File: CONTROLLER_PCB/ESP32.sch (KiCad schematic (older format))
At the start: 3 parts

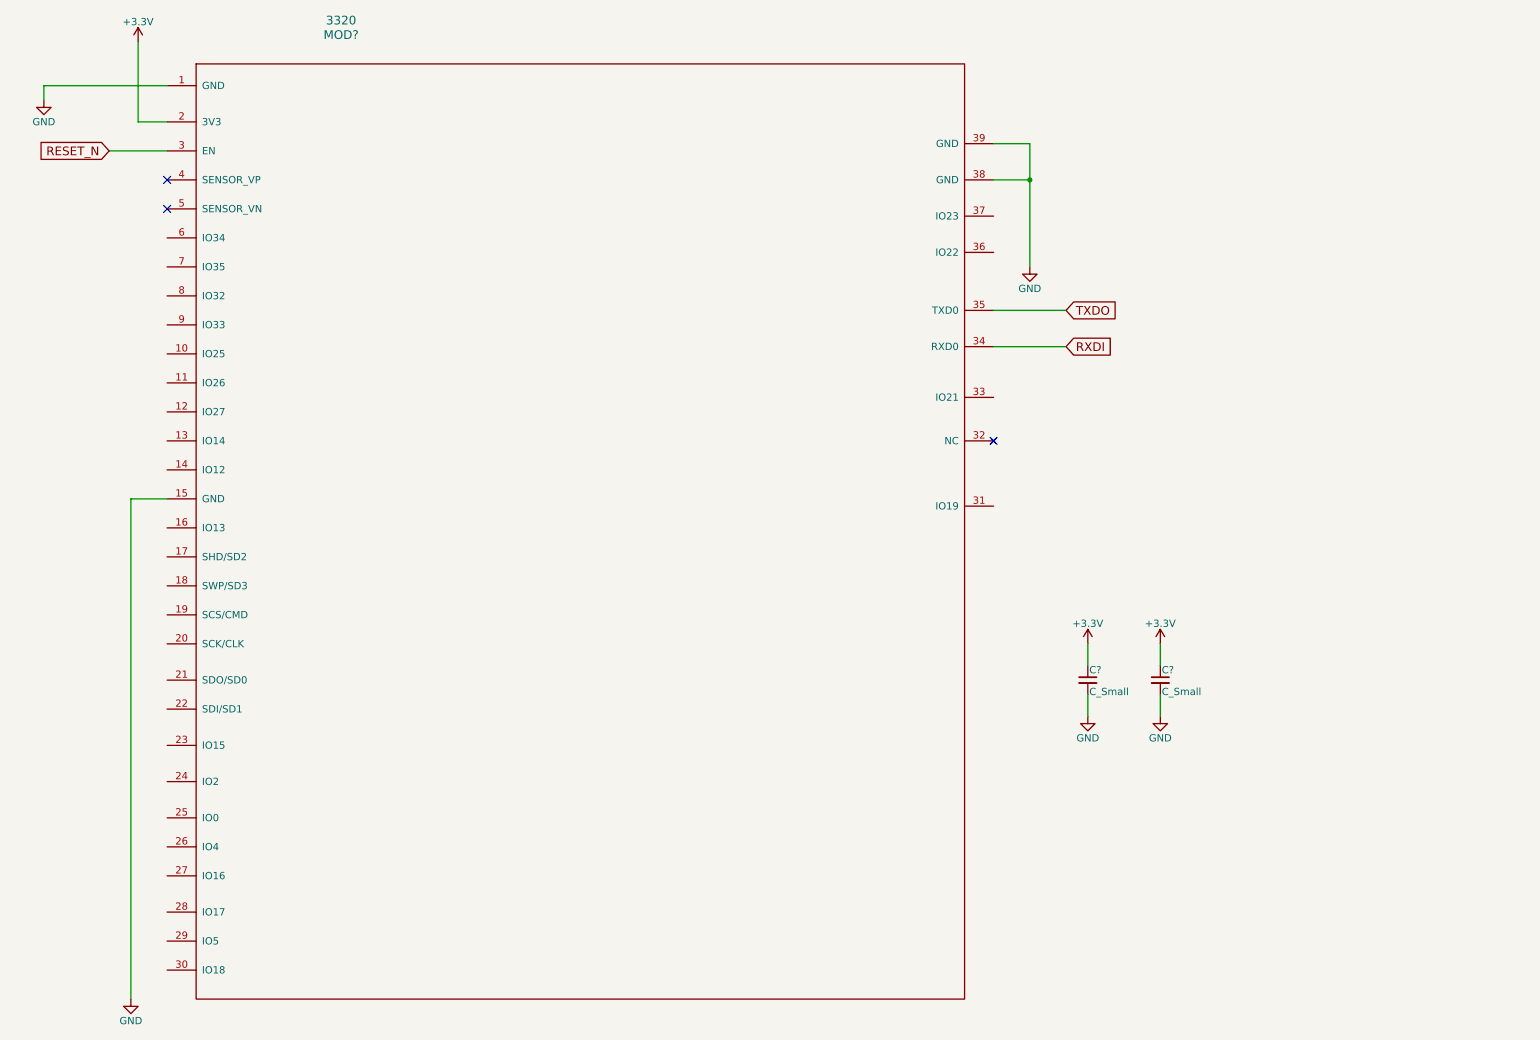
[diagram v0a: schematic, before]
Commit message: Created ESP32 pinout spreadsheet, finished MCU pinout, and added MCU_SUPPORT schematic sheet.
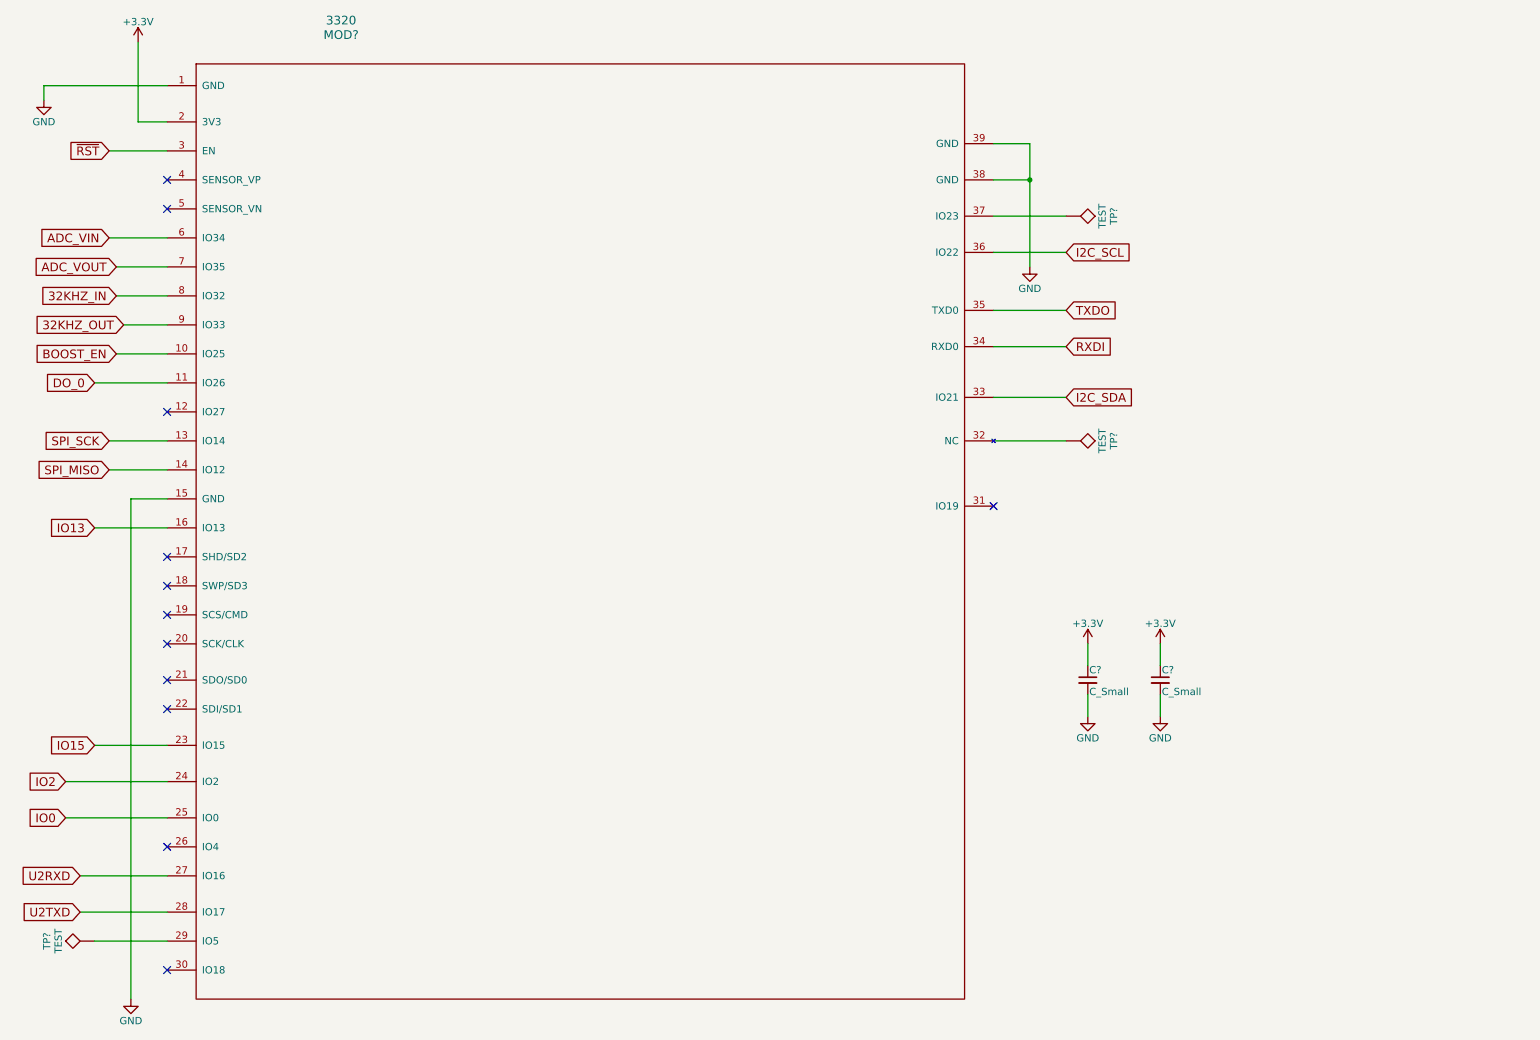
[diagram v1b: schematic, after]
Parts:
- added TP? (x3): TEST, symbol TEST
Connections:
- net BOOST_EN: now reaches MOD?.10 (IO25)
- net DO_0: now reaches MOD?.11 (IO26)
- net SPI_SCK: now reaches MOD?.13 (IO14)
- net SPI_MISO: now reaches MOD?.14 (IO12)
- net IO13: now reaches MOD?.16 (IO13)
- net IO15: now reaches MOD?.23 (IO15)
- net IO2: now reaches MOD?.24 (IO2)
- net IO0: now reaches MOD?.25 (IO0)
- net U2RXD: now reaches MOD?.27 (IO16)
- net U2TXD: now reaches MOD?.28 (IO17)
- net at MOD?.29 (IO5): now also TP?.1
- net at MOD?.32 (NC): now also TP?.1
- net I2C_SDA: now reaches MOD?.33 (IO21)
- net I2C_SCL: now reaches MOD?.36 (IO22)
- net at MOD?.37 (IO23): now also TP?.1
- net ADC_VIN: now reaches MOD?.6 (IO34)
- net ADC_VOUT: now reaches MOD?.7 (IO35)
- net 32KHZ_IN: now reaches MOD?.8 (IO32)
- net 32KHZ_OUT: now reaches MOD?.9 (IO33)
- net RESET_N renamed ~RST
- no-connect marks 3 -> 12
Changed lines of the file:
@@
 $Descr A4 11693 8268
 encoding utf-8
-Sheet 3 3
+Sheet 3 4
 Title ""
 Date ""
@@
 Comment4 ""
 $EndDescr
+$Comp
+L GND #PWR?
+U 1 1 5C5A52E4
+P 600 1150
+F 0 "#PWR?" H 600 900 50  0001 C CNN
+F 1 "GND" H 600 1000 50  0000 C CNN
+F 2 "" H 600 1150 50  0001 C CNN
+F 3 "" H 600 1150 50  0001 C CNN
+	1    600  1150
+	1    0    0    -1
+$EndComp
+$Comp
+L +3.3V #PWR?
+U 1 1 5C5AB14D
+P 1250 750
+F 0 "#PWR?" H 1250 600 50  0001 C CNN
+F 1 "+3.3V" H 1250 890 50  0000 C CNN
+F 2 "" H 1250 750 50  0001 C CNN
+F 3 "" H 1250 750 50  0001 C CNN
+	1    1250 750
+	1    0    0    -1
+$EndComp
+Text GLabel 1050 1500 0    60   Input ~ 0
+~RST
+NoConn ~ 1450 1700
+NoConn ~ 1450 1900
+Wire Wire Line
+	1050 1500 1450 1500
+Wire Wire Line
+	1450 1300 1250 1300
+Wire Wire Line
+	1250 1300 1250 750
+Wire Wire Line
+	1450 1050 600  1050
+Wire Wire Line
+	600  1050 600  1150
+$Comp
+L GND #PWR?
+U 1 1 5C5AB35F
+P 7400 2300
+F 0 "#PWR?" H 7400 2050 50  0001 C CNN
+F 1 "GND" H 7400 2150 50  0000 C CNN
+F 2 "" H 7400 2300 50  0001 C CNN
+F 3 "" H 7400 2300 50  0001 C CNN
+	1    7400 2300
+	1    0    0    -1
+$EndComp
+Wire Wire Line
+	7400 2300 7400 1450
+Wire Wire Line
+	7400 1450 7150 1450
+Wire Wire Line
+	7150 1700 7400 1700
+Connection ~ 7400 1700
+$Comp
+L GND #PWR?
+U 1 1 5C5AB3CE
+P 1200 7350
+F 0 "#PWR?" H 1200 7100 50  0001 C CNN
+F 1 "GND" H 1200 7200 50  0000 C CNN
+F 2 "" H 1200 7350 50  0001 C CNN
+F 3 "" H 1200 7350 50  0001 C CNN
+	1    1200 7350
+	1    0    0    -1
+$EndComp
+Wire Wire Line
+	1200 7350 1200 3900
+Wire Wire Line
+	1200 3900 1450 3900
+Text GLabel 7650 2600 2    60   Input ~ 0
+TXDO
+Text GLabel 7650 2850 2    60   Input ~ 0
+RXDI
+Wire Wire Line
+	7650 2850 7150 2850
+Wire Wire Line
+	7650 2600 7150 2600
+$Comp
+L C_Small C?
+U 1 1 5C5AC1FB
+P 7800 5150
+F 0 "C?" H 7810 5220 50  0000 L CNN
+F 1 "C_Small" H 7810 5070 50  0000 L CNN
+F 2 "" H 7800 5150 50  0001 C CNN
+F 3 "" H 7800 5150 50  0001 C CNN
+	1    7800 5150
+	1    0    0    -1
+$EndComp
+$Comp
+L C_Small C?
+U 1 1 5C5AC279
+P 8300 5150
+F 0 "C?" H 8310 5220 50  0000 L CNN
+F 1 "C_Small" H 8310 5070 50  0000 L CNN
+F 2 "" H 8300 5150 50  0001 C CNN
+F 3 "" H 8300 5150 50  0001 C CNN
+	1    8300 5150
+	1    0    0    -1
+$EndComp
+$Comp
+L GND #PWR?
+U 1 1 5C5AC2C0
+P 7800 5400
+F 0 "#PWR?" H 7800 5150 50  0001 C CNN
+F 1 "GND" H 7800 5250 50  0000 C CNN
+F 2 "" H 7800 5400 50  0001 C CNN
+F 3 "" H 7800 5400 50  0001 C CNN
+	1    7800 5400
+	1    0    0    -1
+$EndComp
+$Comp
+L GND #PWR?
+U 1 1 5C5AC2DA
+P 8300 5400
+F 0 "#PWR?" H 8300 5150 50  0001 C CNN
+F 1 "GND" H 8300 5250 50  0000 C CNN
+F 2 "" H 8300 5400 50  0001 C CNN
+F 3 "" H 8300 5400 50  0001 C CNN
+	1    8300 5400
+	1    0    0    -1
+$EndComp
+$Comp
+L +3.3V #PWR?
+U 1 1 5C5AC2F4
+P 7800 4900
+F 0 "#PWR?" H 7800 4750 50  0001 C CNN
+F 1 "+3.3V" H 7800 5040 50  0000 C CNN
+F 2 "" H 7800 4900 50  0001 C CNN
+F 3 "" H 7800 4900 50  0001 C CNN
+	1    7800 4900
+	1    0    0    -1
+$EndComp
+$Comp
+L +3.3V #PWR?
+U 1 1 5C5AC30E
+P 8300 4900
+F 0 "#PWR?" H 8300 4750 50  0001 C CNN
+F 1 "+3.3V" H 8300 5040 50  0000 C CNN
+F 2 "" H 8300 4900 50  0001 C CNN
+F 3 "" H 8300 4900 50  0001 C CNN
+	1    8300 4900
+	1    0    0    -1
+$EndComp
+Wire Wire Line
+	7800 5050 7800 4900
+Wire Wire Line
+	8300 5050 8300 4900
+Wire Wire Line
+	8300 5250 8300 5400
+Wire Wire Line
+	7800 5250 7800 5400
+Text GLabel 1050 2100 0    60   Input ~ 0
+ADC_VIN
+Text GLabel 1100 2300 0    60   Input ~ 0
+ADC_VOUT
+Wire Wire Line
+	1050 2100 1450 2100
+Wire Wire Line
+	1100 2300 1450 2300
+Text GLabel 1100 2500 0    60   Input ~ 0
+32KHZ_IN
+Text GLabel 1150 2700 0    60   Input ~ 0
+32KHZ_OUT
+Wire Wire Line
+	1100 2500 1450 2500
+Wire Wire Line
+	1150 2700 1450 2700
+Text GLabel 1100 2900 0    60   Input ~ 0
+BOOST_EN
+Wire Wire Line
+	1100 2900 1450 2900
+Text GLabel 950  3100 0    60   Input ~ 0
+DO_0
+Wire Wire Line
+	950  3100 1450 3100
+NoConn ~ 1450 3300
+Text GLabel 1050 3500 0    60   Input ~ 0
+SPI_SCK
+Text GLabel 1050 3700 0    60   Input ~ 0
+SPI_MISO
+Text GLabel 950  4100 0    60   Input ~ 0
+IO13
+Wire Wire Line
+	1050 3500 1450 3500
+Wire Wire Line
+	1050 3700 1450 3700
+Wire Wire Line
+	950  4100 1450 4100
+NoConn ~ 1450 4300
+NoConn ~ 1450 4500
+NoConn ~ 1450 4700
+NoConn ~ 1450 4900
+NoConn ~ 1450 5150
+NoConn ~ 1450 5350
+$Comp
+L TEST TP?
+U 1 1 5C5F05AF
+P 950 6950
+F 0 "TP?" H 950 7250 50  0000 C BNN
+F 1 "TEST" H 950 7200 50  0000 C CNN
+F 2 "" H 950 6950 50  0001 C CNN
+F 3 "" H 950 6950 50  0001 C CNN
+	1    950  6950
+	0    -1   -1   0
+$EndComp
+Text GLabel 750  5850 0    60   Input ~ 0
+IO2
+Wire Wire Line
+	950  5600 1450 5600
+Text GLabel 750  6100 0    60   Input ~ 0
+IO0
+NoConn ~ 1450 6300
+Wire Wire Line
+	750  5850 1450 5850
+Wire Wire Line
+	750  6100 1450 6100
+Text GLabel 850  6500 0    60   Input ~ 0
+U2RXD
+Text GLabel 850  6750 0    60   Input ~ 0
+U2TXD
+Wire Wire Line
+	850  6500 1450 6500
+Wire Wire Line
+	850  6750 1450 6750
+Wire Wire Line
+	950  6950 1450 6950
+NoConn ~ 1450 7150
+NoConn ~ 7150 3950
+$Comp
+L TEST TP?
+U 1 1 5C5F0B08
+P 7650 3500
+F 0 "TP?" H 7650 3800 50  0000 C BNN
+F 1 "TEST" H 7650 3750 50  0000 C CNN
+F 2 "" H 7650 3500 50  0001 C CNN
+F 3 "" H 7650 3500 50  0001 C CNN
+	1    7650 3500
+	0    1    1    0
+$EndComp
 $Comp
 L 3320 MOD?
@@
 	1    0    0    -1
 $EndComp
-$Comp
-L GND #PWR?
-U 1 1 5C5A52E4
-P 600 1150
-F 0 "#PWR?" H 600 900 50  0001 C CNN
-F 1 "GND" H 600 1000 50  0000 C CNN
-F 2 "" H 600 1150 50  0001 C CNN
-F 3 "" H 600 1150 50  0001 C CNN
-	1    600  1150
-	1    0    0    -1
-$EndComp
-$Comp
-L +3.3V #PWR?
-U 1 1 5C5AB14D
-P 1250 750
-F 0 "#PWR?" H 1250 600 50  0001 C CNN
-F 1 "+3.3V" H 1250 890 50  0000 C CNN
-F 2 "" H 1250 750 50  0001 C CNN
-F 3 "" H 1250 750 50  0001 C CNN
-	1    1250 750
-	1    0    0    -1
-$EndComp
-Text GLabel 1050 1500 0    60   Input ~ 0
-RESET_N
-NoConn ~ 1450 1700
-NoConn ~ 1450 1900
-Wire Wire Line
-	1050 1500 1450 1500
-Wire Wire Line
-	1450 1300 1250 1300
-Wire Wire Line
-	1250 1300 1250 750
-Wire Wire Line
-	1450 1050 600  1050
-Wire Wire Line
-	600  1050 600  1150
-NoConn ~ 7150 3500
-$Comp
-L GND #PWR?
-U 1 1 5C5AB35F
-P 7400 2300
-F 0 "#PWR?" H 7400 2050 50  0001 C CNN
-F 1 "GND" H 7400 2150 50  0000 C CNN
-F 2 "" H 7400 2300 50  0001 C CNN
-F 3 "" H 7400 2300 50  0001 C CNN
-	1    7400 2300
-	1    0    0    -1
-$EndComp
-Wire Wire Line
-	7400 2300 7400 1450
-Wire Wire Line
-	7400 1450 7150 1450
-Wire Wire Line
-	7150 1700 7400 1700
-Connection ~ 7400 1700
-$Comp
-L GND #PWR?
-U 1 1 5C5AB3CE
-P 1200 7350
-F 0 "#PWR?" H 1200 7100 50  0001 C CNN
-F 1 "GND" H 1200 7200 50  0000 C CNN
-F 2 "" H 1200 7350 50  0001 C CNN
-F 3 "" H 1200 7350 50  0001 C CNN
-	1    1200 7350
-	1    0    0    -1
-$EndComp
-Wire Wire Line
-	1200 7350 1200 3900
-Wire Wire Line
-	1200 3900 1450 3900
-Text GLabel 7650 2600 2    60   Input ~ 0
-TXDO
-Text GLabel 7650 2850 2    60   Input ~ 0
-RXDI
-Wire Wire Line
-	7650 2850 7150 2850
-Wire Wire Line
-	7650 2600 7150 2600
-$Comp
-L C_Small C?
-U 1 1 5C5AC1FB
-P 7800 5150
-F 0 "C?" H 7810 5220 50  0000 L CNN
-F 1 "C_Small" H 7810 5070 50  0000 L CNN
-F 2 "" H 7800 5150 50  0001 C CNN
-F 3 "" H 7800 5150 50  0001 C CNN
-	1    7800 5150
-	1    0    0    -1
-$EndComp
-$Comp
-L C_Small C?
-U 1 1 5C5AC279
-P 8300 5150
-F 0 "C?" H 8310 5220 50  0000 L CNN
-F 1 "C_Small" H 8310 5070 50  0000 L CNN
-F 2 "" H 8300 5150 50  0001 C CNN
-F 3 "" H 8300 5150 50  0001 C CNN
-	1    8300 5150
-	1    0    0    -1
-$EndComp
-$Comp
-L GND #PWR?
-U 1 1 5C5AC2C0
-P 7800 5400
-F 0 "#PWR?" H 7800 5150 50  0001 C CNN
-F 1 "GND" H 7800 5250 50  0000 C CNN
-F 2 "" H 7800 5400 50  0001 C CNN
-F 3 "" H 7800 5400 50  0001 C CNN
-	1    7800 5400
-	1    0    0    -1
-$EndComp
-$Comp
-L GND #PWR?
-U 1 1 5C5AC2DA
-P 8300 5400
-F 0 "#PWR?" H 8300 5150 50  0001 C CNN
-F 1 "GND" H 8300 5250 50  0000 C CNN
-F 2 "" H 8300 5400 50  0001 C CNN
-F 3 "" H 8300 5400 50  0001 C CNN
-	1    8300 5400
-	1    0    0    -1
-$EndComp
-$Comp
-L +3.3V #PWR?
-U 1 1 5C5AC2F4
-P 7800 4900
-F 0 "#PWR?" H 7800 4750 50  0001 C CNN
-F 1 "+3.3V" H 7800 5040 50  0000 C CNN
-F 2 "" H 7800 4900 50  0001 C CNN
-F 3 "" H 7800 4900 50  0001 C CNN
-	1    7800 4900
-	1    0    0    -1
-$EndComp
-$Comp
-L +3.3V #PWR?
-U 1 1 5C5AC30E
-P 8300 4900
-F 0 "#PWR?" H 8300 4750 50  0001 C CNN
-F 1 "+3.3V" H 8300 5040 50  0000 C CNN
-F 2 "" H 8300 4900 50  0001 C CNN
-F 3 "" H 8300 4900 50  0001 C CNN
-	1    8300 4900
-	1    0    0    -1
-$EndComp
-Wire Wire Line
-	7800 5050 7800 4900
-Wire Wire Line
-	8300 5050 8300 4900
-Wire Wire Line
-	8300 5250 8300 5400
-Wire Wire Line
-	7800 5250 7800 5400
+Wire Wire Line
+	7150 3500 7650 3500
+Text GLabel 7650 3200 2    60   Input ~ 0
+I2C_SDA
+Text GLabel 7650 2200 2    60   Input ~ 0
+I2C_SCL
+Wire Wire Line
+	7650 2200 7150 2200
+Wire Wire Line
+	7650 3200 7150 3200
+$Comp
+L TEST TP?
+U 1 1 5C5F0D76
+P 7650 1950
+F 0 "TP?" H 7650 2250 50  0000 C BNN
+F 1 "TEST" H 7650 2200 50  0000 C CNN
+F 2 "" H 7650 1950 50  0001 C CNN
+F 3 "" H 7650 1950 50  0001 C CNN
+	1    7650 1950
+	0    1    1    0
+$EndComp
+Wire Wire Line
+	7150 1950 7650 1950
+Text GLabel 950  5600 0    60   Input ~ 0
+IO15
 $EndSCHEMATC

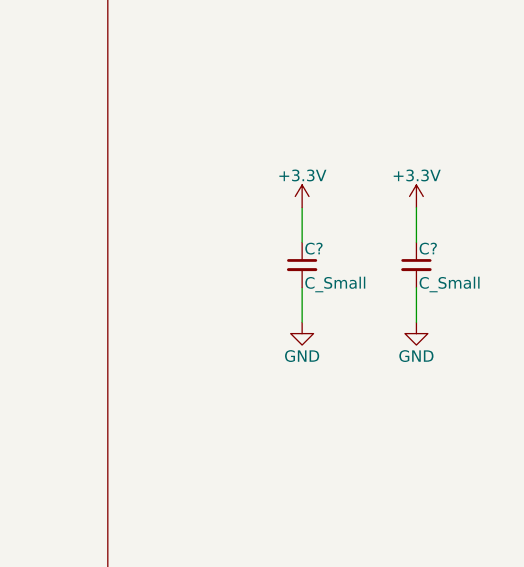
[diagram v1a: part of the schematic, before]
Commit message: Added input filtering, and assigned footprints to most components, several remain.
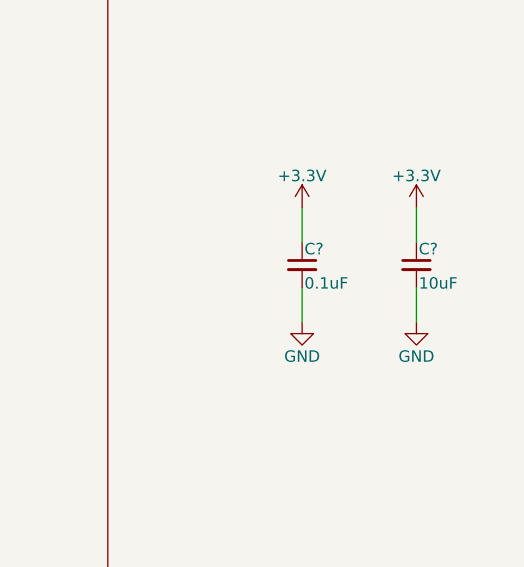
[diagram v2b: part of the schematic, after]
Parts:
- C?: value C_Small -> 0.1uF; footprint (none) -> Capacitors_SMD:C_0603_HandSoldering
- C?: value C_Small -> 10uF; footprint (none) -> Capacitors_SMD:C_0805_HandSoldering
- TP? (x3): footprint (none) -> Measurement_Points:Measurement_Point_Round-SMD-Pad_Small
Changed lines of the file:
@@
 P 7800 5150
 F 0 "C?" H 7810 5220 50  0000 L CNN
-F 1 "C_Small" H 7810 5070 50  0000 L CNN
-F 2 "" H 7800 5150 50  0001 C CNN
+F 1 "0.1uF" H 7810 5070 50  0000 L CNN
+F 2 "Capacitors_SMD:C_0603_HandSoldering" H 7800 5150 50  0001 C CNN
 F 3 "" H 7800 5150 50  0001 C CNN
 	1    7800 5150
@@
 P 8300 5150
 F 0 "C?" H 8310 5220 50  0000 L CNN
-F 1 "C_Small" H 8310 5070 50  0000 L CNN
-F 2 "" H 8300 5150 50  0001 C CNN
+F 1 "10uF" H 8310 5070 50  0000 L CNN
+F 2 "Capacitors_SMD:C_0805_HandSoldering" H 8300 5150 50  0001 C CNN
 F 3 "" H 8300 5150 50  0001 C CNN
 	1    8300 5150
@@
 F 0 "TP?" H 950 7250 50  0000 C BNN
 F 1 "TEST" H 950 7200 50  0000 C CNN
-F 2 "" H 950 6950 50  0001 C CNN
+F 2 "Measurement_Points:Measurement_Point_Round-SMD-Pad_Small" H 950 6950 50  0001 C CNN
 F 3 "" H 950 6950 50  0001 C CNN
 	1    950  6950
@@
 F 0 "TP?" H 7650 3800 50  0000 C BNN
 F 1 "TEST" H 7650 3750 50  0000 C CNN
-F 2 "" H 7650 3500 50  0001 C CNN
+F 2 "Measurement_Points:Measurement_Point_Round-SMD-Pad_Small" H 7650 3500 50  0001 C CNN
 F 3 "" H 7650 3500 50  0001 C CNN
 	1    7650 3500
@@
 F 0 "TP?" H 7650 2250 50  0000 C BNN
 F 1 "TEST" H 7650 2200 50  0000 C CNN
-F 2 "" H 7650 1950 50  0001 C CNN
+F 2 "Measurement_Points:Measurement_Point_Round-SMD-Pad_Small" H 7650 1950 50  0001 C CNN
 F 3 "" H 7650 1950 50  0001 C CNN
 	1    7650 1950
